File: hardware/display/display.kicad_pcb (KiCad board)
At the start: 4 copper layers, 98 x 67 mm, 425 parts, among them J1 Power Connector, J2 Data Connector

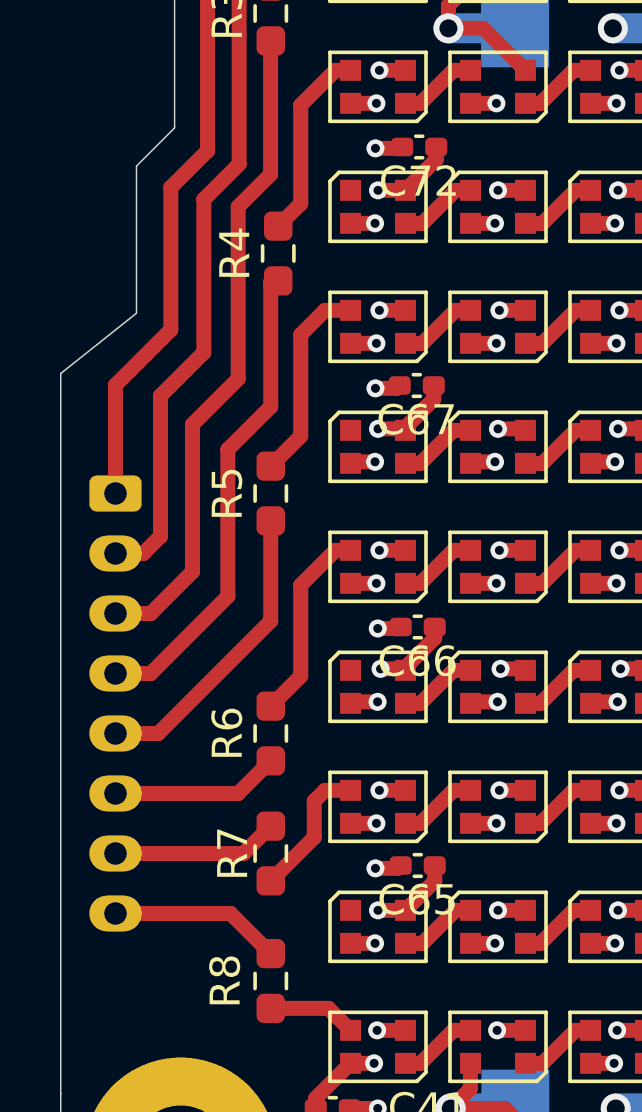
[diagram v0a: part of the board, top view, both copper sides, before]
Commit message: Updated Motherboard and Minor Display Changes
Updated Joystick Position, Moved Display Board Port

other small fixes
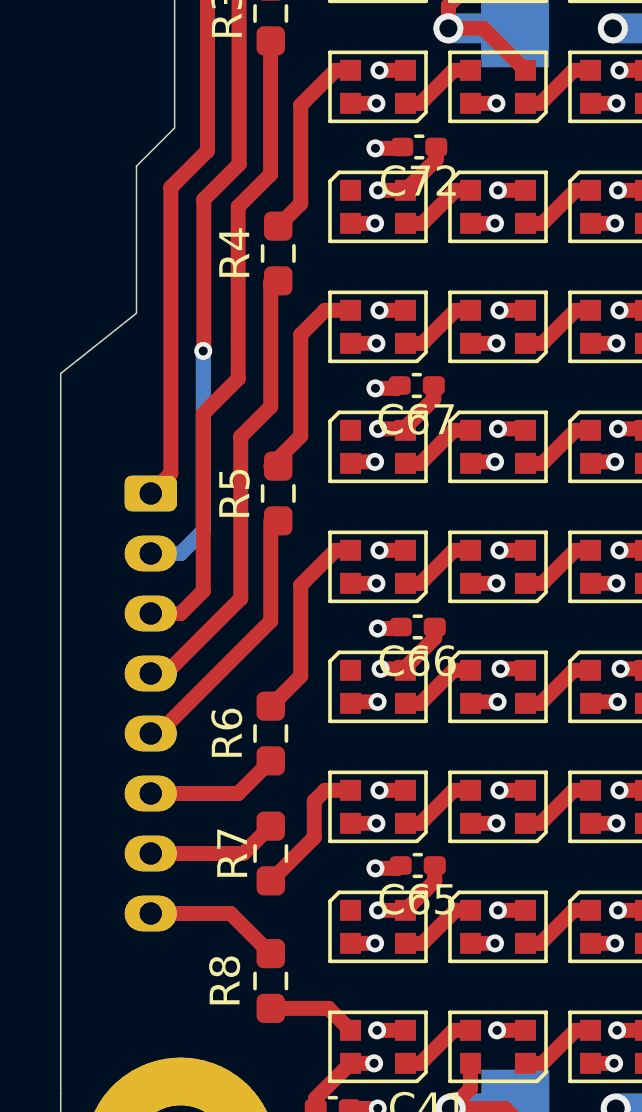
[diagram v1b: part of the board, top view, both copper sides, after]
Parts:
- moved J2 1.18 mm to (10.0, 53.0)
- moved R5 0.25 mm to (14.2, 53.0)
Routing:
- net DIN8: track 5.73 -> 4.55 mm
- net DIN7: track 5.55 -> 4.38 mm
- net DIN6: track 5.63 -> 4.45 mm
- net DIN5: track 10.1 -> 8.89 mm
- net DIN4: track 16.2 -> 15.3 mm
- net DIN3: track 21.9 -> 21.3 mm
- net DIN2: track 27.8 -> 27.4 mm, vias 0 -> 1
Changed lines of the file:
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@@
 	(footprint "Resistor_SMD:R_0603_1608Metric_Pad0.98x0.95mm_HandSolder"
 		(layer "F.Cu")
-		(at 14 53 90)
+		(at 14.25 53 90)
 		(descr "Resistor SMD 0603 (1608 Metric), square (rectangular) end terminal, IPC-7351 nominal with elongated pad for handsoldering. (Body size source: IPC-SM-782 page 72, https://www.pcb-3d.com/wordpress/wp-content/uploads/ipc-sm-782a_amendment_1_and_2.pdf), generated with kicad-footprint-generator")
 		(tags "resistor handsolder")
@@
 	(footprint "Connector_JST:JST_PH_S8B-PH-K_1x08_P2.00mm_Horizontal"
 		(layer "B.Cu")
-		(at 8.825 53 -90)
+		(at 10 53 -90)
 		(descr "JST PH series connector, S8B-PH-K (http://www.jst-mfg.com/product/pdf/eng/ePH.pdf), generated with kicad-footprint-generator")
 		(tags "connector JST PH horizontal")
@@
 	)
 	(segment
-		(start 12.915 49.175)
-		(end 11.39 50.7)
+		(start 13.995 42.36)
+		(end 12.915 43.44)
 		(width 0.5)
 		(layer "F.Cu")
@@
 	)
 	(segment
-		(start 12.915 43.44)
-		(end 12.915 49.175)
+		(start 13.995 37.9175)
+		(end 13.995 42.36)
 		(width 0.5)
 		(layer "F.Cu")
@@
 	)
 	(segment
-		(start 10 57)
-		(end 8.825 57)
+		(start 14 37.9125)
+		(end 13.995 37.9175)
 		(width 0.5)
 		(layer "F.Cu")
@@
 	)
 	(segment
-		(start 13.995 37.9175)
-		(end 13.995 42.36)
+		(start 12.915 43.44)
+		(end 12.915 49.175)
 		(width 0.5)
 		(layer "F.Cu")
@@
 	)
 	(segment
-		(start 14 37.9125)
-		(end 13.995 37.9175)
+		(start 11 57)
+		(end 10 57)
 		(width 0.5)
 		(layer "F.Cu")
@@
 	)
 	(segment
-		(start 13.995 42.36)
-		(end 12.915 43.44)
+		(start 11.75 56.25)
+		(end 11 57)
 		(width 0.5)
 		(layer "F.Cu")
@@
 	)
 	(segment
-		(start 11.39 55.61)
-		(end 10 57)
+		(start 12.915 49.175)
+		(end 11.75 50.34)
 		(width 0.5)
 		(layer "F.Cu")
@@
 	)
 	(segment
-		(start 11.39 50.7)
-		(end 11.39 55.61)
+		(start 11.75 50.34)
+		(end 11.75 56.25)
 		(width 0.5)
 		(layer "F.Cu")
@@
 	(segment
 		(start 12.6625 67)
-		(end 14 68.3375)
+		(end 10 67)
 		(width 0.5)
 		(layer "F.Cu")
@@
 	)
 	(segment
-		(start 8.825 67)
-		(end 12.6625 67)
+		(start 12.6625 67)
+		(end 14 68.3375)
 		(width 0.5)
 		(layer "F.Cu")
@@
 	)
 	(segment
-		(start 8.825 63)
-		(end 12.9125 63)
+		(start 12.9125 63)
+		(end 14 61.9125)
 		(width 0.5)
 		(layer "F.Cu")
@@
 	(segment
 		(start 12.9125 63)
-		(end 14 61.9125)
+		(end 10 63)
 		(width 0.5)
 		(layer "F.Cu")
@@
 	)
 	(segment
-		(start 8.825 61)
-		(end 10.25 61)
+		(start 10.25 61)
+		(end 10 61)
 		(width 0.5)
 		(layer "F.Cu")
@@
 	)
 	(segment
-		(start 10.25 61)
-		(end 14 57.25)
+		(start 14 57.25)
+		(end 10.25 61)
 		(width 0.5)
 		(layer "F.Cu")
@@
 	)
 	(segment
-		(start 8.825 65)
-		(end 13.0875 65)
+		(start 13.0875 65)
+		(end 10 65)
 		(width 0.5)
 		(layer "F.Cu")
@@
 	)
 	(segment
-		(start 12.57 51.535)
-		(end 14 50.105)
+		(start 14 50.105)
+		(end 14 46)
 		(width 0.5)
 		(layer "F.Cu")
@@
 	)
 	(segment
-		(start 14.0875 45.9125)
-		(end 14 46)
+		(start 10.5 59)
+		(end 13 56.5)
 		(width 0.5)
 		(layer "F.Cu")
@@
 	)
 	(segment
-		(start 12.57 56.43)
-		(end 12.57 51.535)
+		(start 10 59)
+		(end 10.5 59)
 		(width 0.5)
 		(layer "F.Cu")
@@
 	)
 	(segment
-		(start 14 50.105)
+		(start 14.0875 45.9125)
 		(end 14 46)
 		(width 0.5)
@@
 	)
 	(segment
-		(start 8.825 59)
-		(end 10 59)
+		(start 13 56.5)
+		(end 13 51.105)
 		(width 0.5)
 		(layer "F.Cu")
@@
 	)
 	(segment
-		(start 14 46)
-		(end 14 45.9125)
+		(start 13 51.105)
+		(end 14 50.105)
 		(width 0.5)
 		(layer "F.Cu")
@@
 	)
 	(segment
-		(start 10 59)
-		(end 12.57 56.43)
+		(start 14 46)
+		(end 14 45.9125)
 		(width 0.5)
 		(layer "F.Cu")
@@
 	)
 	(segment
-		(start 10.67 42.8)
-		(end 11.892 41.578)
+		(start 10 53)
+		(end 10.67 52.33)
 		(width 0.5)
 		(layer "F.Cu")
@@
 	)
 	(segment
-		(start 10.67 47.54)
+		(start 10.67 52.33)
 		(end 10.67 42.8)
 		(width 0.5)
@@
 	)
 	(segment
-		(start 11.892 41.578)
-		(end 11.892 24.0205)
-		(width 0.5)
-		(layer "F.Cu")
-		(net 66)
-	)
-	(segment
-		(start 8.825 53)
-		(end 8.825 49.385)
+		(start 11.892 24.0205)
+		(end 14 21.9125)
 		(width 0.5)
 		(layer "F.Cu")
@@
 	)
 	(segment
-		(start 11.892 24.0205)
-		(end 14 21.9125)
+		(start 10.67 42.8)
+		(end 11.892 41.578)
 		(width 0.5)
 		(layer "F.Cu")
@@
 	)
 	(segment
-		(start 8.825 49.385)
-		(end 10.67 47.54)
+		(start 11.892 41.578)
+		(end 11.892 24.0205)
 		(width 0.5)
 		(layer "F.Cu")
@@
 	)
 	(segment
-		(start 8.825 55)
-		(end 9.75 55)
+		(start 12.945 30.9675)
+		(end 14 29.9125)
 		(width 0.5)
 		(layer "F.Cu")
@@
 	)
 	(segment
-		(start 10.325 54.425)
-		(end 10.325 49.745)
+		(start 11.77 43.2)
+		(end 12.945 42.025)
 		(width 0.5)
 		(layer "F.Cu")
 		(net 67)
 	)
-	(segment
-		(start 10.325 49.745)
-		(end 11.77 48.3)
-		(width 0.5)
-		(layer "F.Cu")
+	(via
+		(at 11.75 48.25)
+		(size 0.6)
+		(drill 0.3)
+		(layers "F.Cu" "B.Cu")
 		(net 67)
 	)
 	(segment
-		(start 12.945 30.9675)
-		(end 14 29.9125)
+		(start 11.75 54.25)
+		(end 11.75 48.25)
 		(width 0.5)
-		(layer "F.Cu")
+		(layer "B.Cu")
 		(net 67)
 	)
 	(segment
-		(start 9.75 55)
-		(end 10.325 54.425)
+		(start 11 55)
+		(end 11.75 54.25)
 		(width 0.5)
-		(layer "F.Cu")
+		(layer "B.Cu")
 		(net 67)
 	)
 	(segment
-		(start 11.77 43.2)
-		(end 12.945 42.025)
+		(start 10 55)
+		(end 11 55)
 		(width 0.5)
-		(layer "F.Cu")
+		(layer "B.Cu")
 		(net 67)
 	)

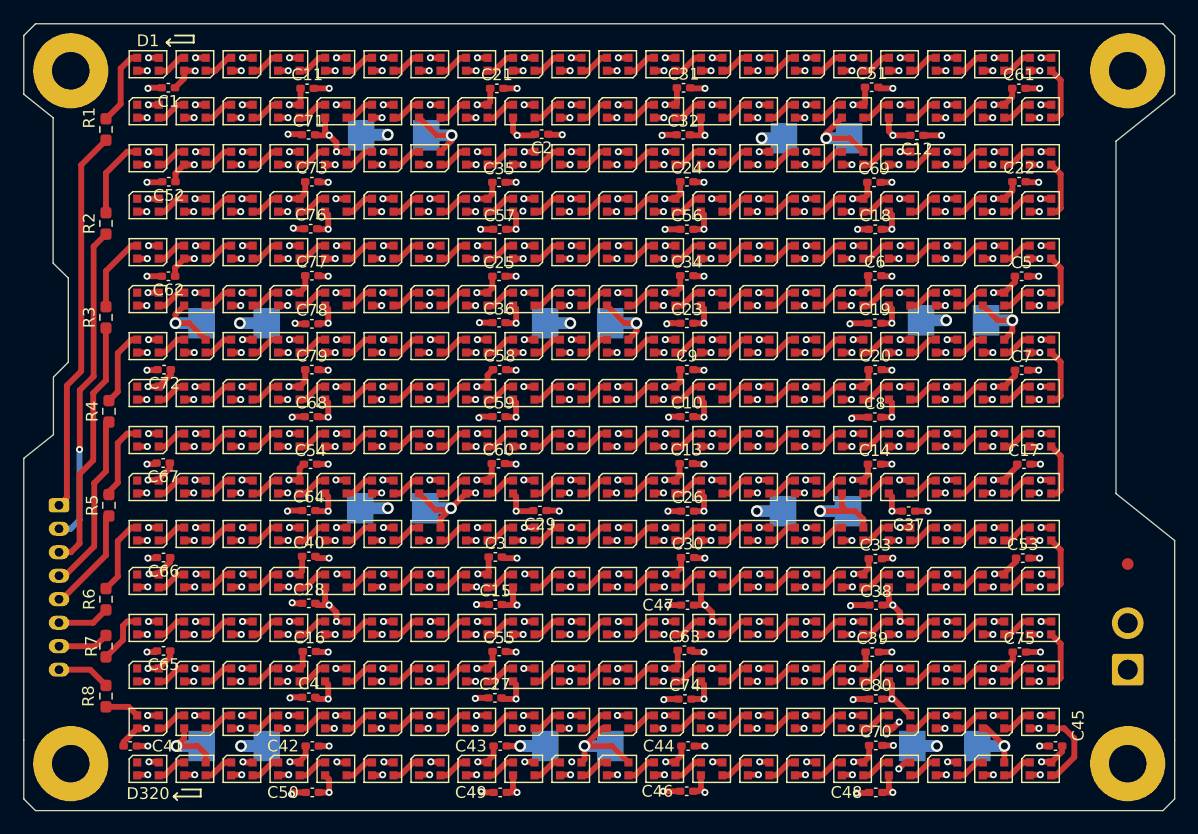
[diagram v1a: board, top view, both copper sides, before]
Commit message: ERC and DRC Checks
Made slight modifications to schematics and layouts to ensure ERCs and DRCs pass on both boards.

Made some exclusions for irrelevant warnings.
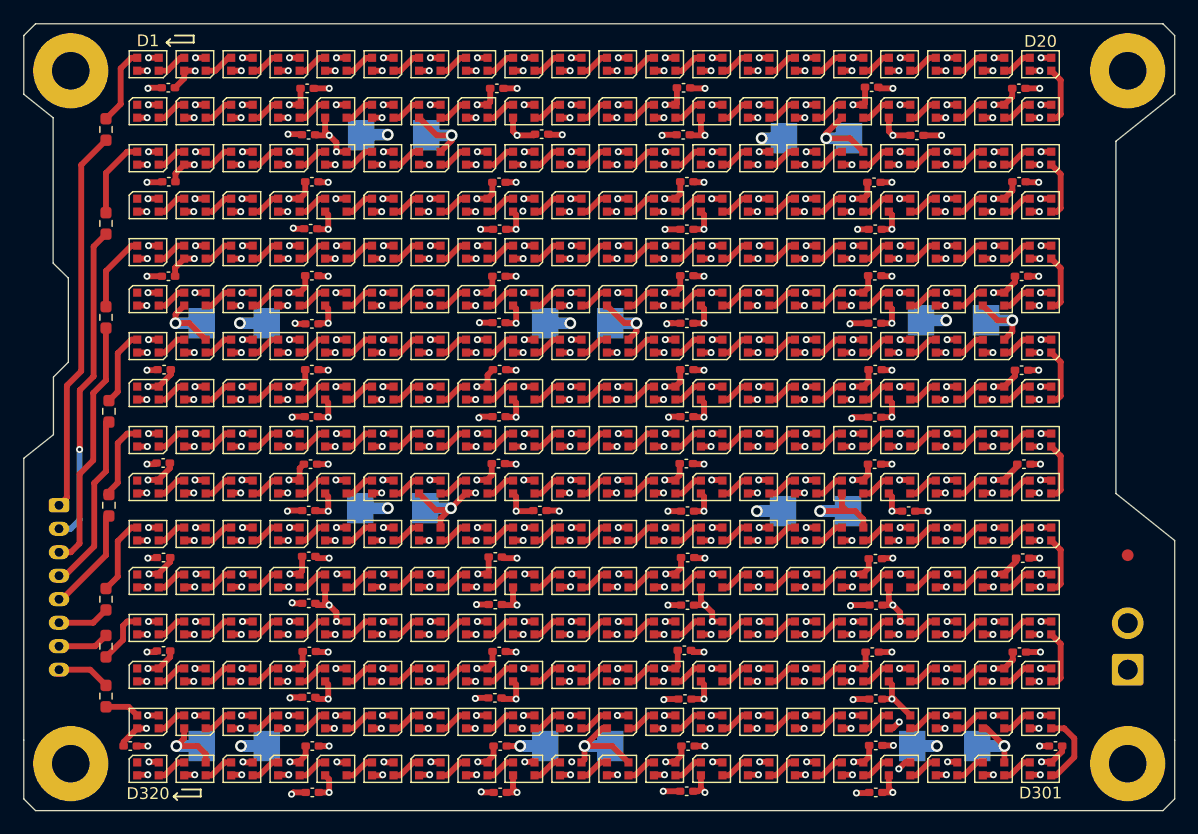
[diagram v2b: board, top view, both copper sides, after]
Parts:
- moved FID1 0.75 mm to (101.0, 57.2)
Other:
- board text added: "D20"
- board text added: "D301"
